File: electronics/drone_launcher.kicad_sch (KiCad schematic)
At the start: 30 parts, among them J1 Servos F1, J10 I2C IMU, J11 I2C GPS, J12 I2C LCD, J13 BTNS F1R1, J14 BTNS F1R2, J15 BTNS F2R1, J16 BTNS F2R2, J17 BTNS F3R1, J18 BTNS F3R2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

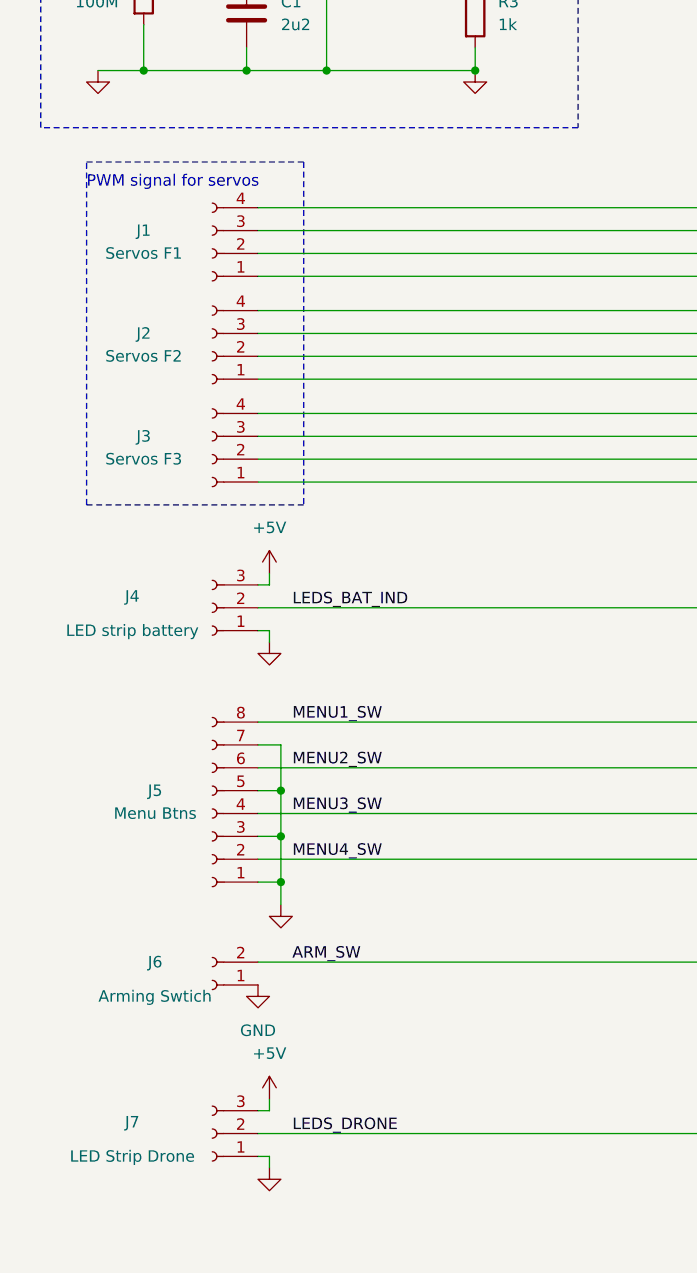
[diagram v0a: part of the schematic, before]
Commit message: added labels and initial pcb layout
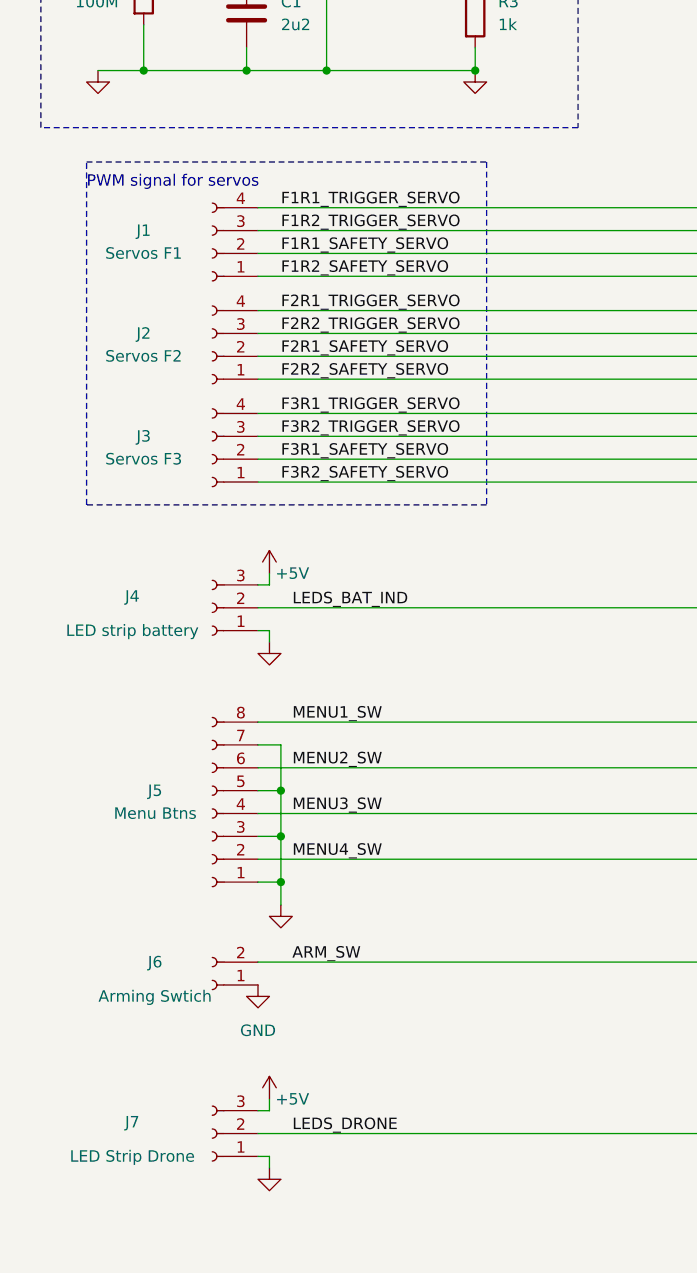
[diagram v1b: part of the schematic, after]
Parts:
- J1, J10, J11, J12, J2, J3, J8: footprint (none) -> Connector_JST:JST_XH_B4B-XH-A_1x04_P2.50mm_Vertical
- J13, J14, J15, J16, J17, J18: footprint (none) -> Connector_JST:JST_XH_B6B-XH-A_1x06_P2.50mm_Vertical
- J4, J7: footprint (none) -> Connector_JST:JST_XH_B3B-XH-A_1x03_P2.50mm_Vertical
- J5: footprint (none) -> Connector_JST:JST_XH_B8B-XH-A_1x08_P2.50mm_Vertical
- J6, J9: footprint (none) -> Connector_JST:JST_XH_B2B-XH-A_1x02_P2.50mm_Vertical
- U2: footprint (none) -> teensy:Teensy41
- U3: footprint (none) -> Adafruit_MCP23017_Breakout:Adafruit_MCP23017_Breakout
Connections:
- net F2R2_SAFETY_SERVO: now reaches J2.1 (Pin_1), U2.7 (5_IN2)
- net F2R1_SAFETY_SERVO: now reaches J2.2 (Pin_2), U2.6 (4_BCLK2)
- net F2R2_TRIGGER_SERVO: now reaches J2.3 (Pin_3), U2.5 (3_LRCLK2)
- net F2R1_TRIGGER_SERVO: now reaches J2.4 (Pin_4), U2.4 (2_OUT2)
- net F3R2_SAFETY_SERVO: now reaches J3.1 (Pin_1), U2.11 (9_OUT1C)
- net F3R1_SAFETY_SERVO: now reaches J3.2 (Pin_2), U2.10 (8_TX2_IN1)
- net F3R2_TRIGGER_SERVO: now reaches J3.3 (Pin_3), U2.9 (7_RX2_OUT1A)
- net F3R1_TRIGGER_SERVO: now reaches J3.4 (Pin_4), U2.8 (6_OUT1D)
- net F1R1_TRIGGER_SERVO: now reaches J1.4 (Pin_4), U2.36 (14_A0_TX3_SPDIF_OUT)
- net F1R2_TRIGGER_SERVO: now reaches J1.3 (Pin_3), U2.37 (15_A1_RX3_SPDIF_IN)
- net F1R1_SAFETY_SERVO: now reaches J1.2 (Pin_2), U2.44 (22_A8_CTX1)
- net F1R2_SAFETY_SERVO: now reaches J1.1 (Pin_1), U2.45 (23_A9_CRX1_MCLK1)
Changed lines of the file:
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@@
     (fill (type none))
   )
-  (rectangle (start 22.86 74.93) (end 46.99 113.03)
+  (rectangle (start 22.86 74.93) (end 67.31 113.03)
     (stroke (width 0) (type dash))
     (fill (type none))
@@
     (effects (font (size 1.27 1.27)) (justify left bottom))
   )
+  (label "F2R2_TRIGGER_SERVO" (at 44.45 93.98 0) (fields_autoplaced)
+    (effects (font (size 1.27 1.27)) (justify left bottom))
+  )
   (label "F3R1_SAFETY_SW" (at 354.33 173.99 0) (fields_autoplaced)
     (effects (font (size 1.27 1.27)) (justify left bottom))
@@
     (effects (font (size 1.27 1.27)) (justify left bottom))
   )
+  (label "F2R1_TRIGGER_SERVO" (at 44.45 91.44 0) (fields_autoplaced)
+    (effects (font (size 1.27 1.27)) (justify left bottom))
+  )
   (label "F3R2_TOP_SW" (at 354.33 189.23 0) (fields_autoplaced)
     (effects (font (size 1.27 1.27)) (justify left bottom))
@@
     (effects (font (size 1.27 1.27)) (justify left bottom))
   )
+  (label "F3R1_SAFETY_SERVO" (at 44.45 107.95 0) (fields_autoplaced)
+    (effects (font (size 1.27 1.27)) (justify left bottom))
+  )
   (label "SCL" (at 231.14 68.58 0) (fields_autoplaced)
     (effects (font (size 1.27 1.27)) (justify left bottom))
@@
     (effects (font (size 1.27 1.27)) (justify left bottom))
   )
+  (label "F3R2_SAFETY_SERVO" (at 44.45 110.49 0) (fields_autoplaced)
+    (effects (font (size 1.27 1.27)) (justify left bottom))
+  )
   (label "F2R2_SAFETY_SW" (at 257.81 229.87 0) (fields_autoplaced)
     (effects (font (size 1.27 1.27)) (justify left bottom))
@@
     (effects (font (size 1.27 1.27)) (justify left bottom))
   )
+  (label "F2R2_SAFETY_SERVO" (at 44.45 99.06 0) (fields_autoplaced)
+    (effects (font (size 1.27 1.27)) (justify left bottom))
+  )
   (label "MENU3_SW" (at 45.72 147.32 0) (fields_autoplaced)
     (effects (font (size 1.27 1.27)) (justify left bottom))
@@
   )
   (label "LEDS_BAT_IND" (at 45.72 124.46 0) (fields_autoplaced)
+    (effects (font (size 1.27 1.27)) (justify left bottom))
+  )
+  (label "F1R1_SAFETY_SERVO" (at 44.45 85.09 0) (fields_autoplaced)
     (effects (font (size 1.27 1.27)) (justify left bottom))
   )
@@
     (effects (font (size 1.27 1.27)) (justify left bottom))
   )
+  (label "F2R1_SAFETY_SERVO" (at 44.45 96.52 0) (fields_autoplaced)
+    (effects (font (size 1.27 1.27)) (justify left bottom))
+  )
+  (label "F1R1_TRIGGER_SERVO" (at 44.45 80.01 0) (fields_autoplaced)
+    (effects (font (size 1.27 1.27)) (justify left bottom))
+  )
   (label "MENU2_SW" (at 45.72 142.24 0) (fields_autoplaced)
     (effects (font (size 1.27 1.27)) (justify left bottom))
@@
   )
   (label "F1R1_TOP_SW" (at 354.33 76.2 0) (fields_autoplaced)
+    (effects (font (size 1.27 1.27)) (justify left bottom))
+  )
+  (label "F1R2_SAFETY_SERVO" (at 44.45 87.63 0) (fields_autoplaced)
     (effects (font (size 1.27 1.27)) (justify left bottom))
   )
@@
     (effects (font (size 1.27 1.27)) (justify left bottom))
   )
+  (label "F1R2_TRIGGER_SERVO" (at 44.45 82.55 0) (fields_autoplaced)
+    (effects (font (size 1.27 1.27)) (justify left bottom))
+  )
   (label "MENU4_SW" (at 45.72 152.4 0) (fields_autoplaced)
     (effects (font (size 1.27 1.27)) (justify left bottom))
@@
   )
   (label "MENU1_SW" (at 45.72 137.16 0) (fields_autoplaced)
+    (effects (font (size 1.27 1.27)) (justify left bottom))
+  )
+  (label "F3R2_TRIGGER_SERVO" (at 44.45 105.41 0) (fields_autoplaced)
+    (effects (font (size 1.27 1.27)) (justify left bottom))
+  )
+  (label "F3R1_TRIGGER_SERVO" (at 44.45 102.87 0) (fields_autoplaced)
     (effects (font (size 1.27 1.27)) (justify left bottom))
   )
@@
       (effects (font (size 1.27 1.27)))
     )
-    (property "Footprint" "" (at 287.02 46.99 0)
+    (property "Footprint" "Connector_JST:JST_XH_B4B-XH-A_1x04_P2.50mm_Vertical" (at 287.02 46.99 0)
       (effects (font (size 1.27 1.27)) hide)
     )
@@
       (effects (font (size 1.27 1.27)))
     )
-    (property "Footprint" "" (at 36.83 96.52 0)
+    (property "Footprint" "Connector_JST:JST_XH_B4B-XH-A_1x04_P2.50mm_Vertical" (at 36.83 96.52 0)
       (effects (font (size 1.27 1.27)) hide)
     )
@@
       (effects (font (size 1.27 1.27)))
     )
-    (property "Footprint" "" (at 36.83 107.95 0)
+    (property "Footprint" "Connector_JST:JST_XH_B4B-XH-A_1x04_P2.50mm_Vertical" (at 36.83 107.95 0)
       (effects (font (size 1.27 1.27)) hide)
     )
@@
       (effects (font (size 1.27 1.27)) (justify left))
     )
-    (property "Footprint" "" (at 378.46 173.99 0)
+    (property "Footprint" "Connector_JST:JST_XH_B6B-XH-A_1x06_P2.50mm_Vertical" (at 378.46 173.99 0)
       (effects (font (size 1.27 1.27)) hide)
     )
@@
       (effects (font (size 1.27 1.27)))
     )
-    (property "Footprint" "" (at 36.83 182.88 0)
+    (property "Footprint" "Connector_JST:JST_XH_B3B-XH-A_1x03_P2.50mm_Vertical" (at 36.83 182.88 0)
       (effects (font (size 1.27 1.27)) hide)
     )
@@
       (effects (font (size 1.27 1.27)) (justify left))
     )
-    (property "Footprint" "" (at 378.46 149.86 0)
+    (property "Footprint" "Connector_JST:JST_XH_B6B-XH-A_1x06_P2.50mm_Vertical" (at 378.46 149.86 0)
       (effects (font (size 1.27 1.27)) hide)
     )
@@
       (effects (font (size 1.27 1.27)))
     )
-    (property "Footprint" "" (at 299.72 46.99 0)
+    (property "Footprint" "Connector_JST:JST_XH_B4B-XH-A_1x04_P2.50mm_Vertical" (at 299.72 46.99 0)
       (effects (font (size 1.27 1.27)) hide)
     )
@@
       (effects (font (size 1.27 1.27)) (justify left))
     )
-    (property "Footprint" "" (at 378.46 101.6 0)
+    (property "Footprint" "Connector_JST:JST_XH_B6B-XH-A_1x06_P2.50mm_Vertical" (at 378.46 101.6 0)
       (effects (font (size 1.27 1.27)) hide)
     )
@@
       (effects (font (size 1.27 1.27)) (justify left))
     )
-    (property "Footprint" "" (at 378.46 81.28 0)
+    (property "Footprint" "Connector_JST:JST_XH_B6B-XH-A_1x06_P2.50mm_Vertical" (at 378.46 81.28 0)
       (effects (font (size 1.27 1.27)) hide)
     )
@@
       (effects (font (size 1.27 1.27)))
     )
-    (property "Footprint" "" (at 36.83 166.37 0)
+    (property "Footprint" "Connector_JST:JST_XH_B2B-XH-A_1x02_P2.50mm_Vertical" (at 36.83 166.37 0)
       (effects (font (size 1.27 1.27)) hide)
     )
@@
       (effects (font (size 1.27 1.27)))
     )
-    (property "Footprint" "" (at 243.84 46.99 0)
+    (property "Footprint" "Connector_JST:JST_XH_B4B-XH-A_1x04_P2.50mm_Vertical" (at 243.84 46.99 0)
       (effects (font (size 1.27 1.27)) hide)
     )
@@
       (effects (font (size 1.27 1.27)) (justify right))
     )
-    (property "Footprint" "" (at 256.54 46.99 0)
+    (property "Footprint" "Connector_JST:JST_XH_B2B-XH-A_1x02_P2.50mm_Vertical" (at 256.54 46.99 0)
       (effects (font (size 1.27 1.27)) hide)
     )
@@
       (effects (font (size 1.27 1.27)))
     )
-    (property "Footprint" "" (at 36.83 124.46 0)
+    (property "Footprint" "Connector_JST:JST_XH_B3B-XH-A_1x03_P2.50mm_Vertical" (at 36.83 124.46 0)
       (effects (font (size 1.27 1.27)) hide)
     )
@@
   )
   (symbol (lib_id "power:+5V") (at 43.18 179.07 0) (unit 1)
-    (in_bom yes) (on_board yes) (dnp no) (fields_autoplaced)
+    (in_bom yes) (on_board yes) (dnp no)
     (property "Reference" "#PWR06" (at 43.18 182.88 0)
       (effects (font (size 1.27 1.27)) hide)
     )
-    (property "Value" "+5V" (at 43.18 173.99 0)
+    (property "Value" "+5V" (at 45.72 179.07 0)
       (effects (font (size 1.27 1.27)))
     )
@@
       (effects (font (size 1.27 1.27)))
     )
-    (property "Footprint" "" (at 273.05 46.99 0)
+    (property "Footprint" "Connector_JST:JST_XH_B4B-XH-A_1x04_P2.50mm_Vertical" (at 273.05 46.99 0)
       (effects (font (size 1.27 1.27)) hide)
     )
@@
   )
   (symbol (lib_id "power:+5V") (at 43.18 120.65 0) (unit 1)
-    (in_bom yes) (on_board yes) (dnp no) (fields_autoplaced)
+    (in_bom yes) (on_board yes) (dnp no)
     (property "Reference" "#PWR04" (at 43.18 124.46 0)
       (effects (font (size 1.27 1.27)) hide)
     )
-    (property "Value" "+5V" (at 43.18 115.57 0)
+    (property "Value" "+5V" (at 45.72 120.65 0)
       (effects (font (size 1.27 1.27)))
     )
@@
       (effects (font (size 1.27 1.27)))
     )
-    (property "Footprint" "" (at 158.75 128.27 0)
+    (property "Footprint" "teensy:Teensy41" (at 158.75 128.27 0)
       (effects (font (size 1.27 1.27)) hide)
     )
@@
       (effects (font (size 1.27 1.27)))
     )
-    (property "Footprint" "" (at 36.83 85.09 0)
+    (property "Footprint" "Connector_JST:JST_XH_B4B-XH-A_1x04_P2.50mm_Vertical" (at 36.83 85.09 0)
       (effects (font (size 1.27 1.27)) hide)
     )
@@
       (effects (font (size 1.27 1.27)) (justify left))
     )
-    (property "Footprint" "" (at 378.46 129.54 0)
+    (property "Footprint" "Connector_JST:JST_XH_B6B-XH-A_1x06_P2.50mm_Vertical" (at 378.46 129.54 0)
       (effects (font (size 1.27 1.27)) hide)
     )
@@
       (effects (font (size 1.27 1.27)))
     )
-    (property "Footprint" "" (at 36.83 147.32 0)
+    (property "Footprint" "Connector_JST:JST_XH_B8B-XH-A_1x08_P2.50mm_Vertical" (at 40.64 157.48 0)
       (effects (font (size 1.27 1.27)) hide)
     )
@@
       (effects (font (size 1.27 1.27)) (justify left))
     )
-    (property "Footprint" "" (at 378.46 194.31 0)
+    (property "Footprint" "Connector_JST:JST_XH_B6B-XH-A_1x06_P2.50mm_Vertical" (at 378.46 194.31 0)
       (effects (font (size 1.27 1.27)) hide)
     )
@@
       (effects (font (size 1.27 1.27)))
     )
-    (property "Footprint" "" (at 279.4 203.2 0)
-      (effects (font (size 1.27 1.27)) hide)
-    )
+    (property "Footprint" "Adafruit_MCP23017_Breakout:Adafruit_MCP23017_Breakout" (at 279.4 203.2 0)
+      (effects (font (size 1.27 1.27)) hide)
+    )

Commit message: improved routing and new footprints
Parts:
- removed 111, 112, 12: ~, drone_launcher:MOUNTINGHOLE_3.0_PLATED_VIAS, symbol drone_launcher-eagle-import:MOUNTINGHOLE
- added J19: GPS, Connector_JST:JST_XH_B6B-XH-A_1x06_P2.50mm_Vertical, symbol Connector:Conn_01x06_Socket
- added J20: XT60-M, AMASS_XT60-M, symbol XT60-M:XT60-M
- added MH2, MH3, MH4: ~, MountingHole:MountingHole_3.2mm_M3, symbol drone_launcher-eagle-import:MOUNTINGHOLE
- C1: footprint (none) -> Capacitor_SMD:C_1206_3216Metric
- D1: footprint (none) -> LED_SMD:LED_1206_3216Metric
- J11: value I2C GPS -> I2C LCD
- J12: value I2C LCD -> I2C Extra
- MH1: renamed from 11; footprint drone_launcher:MOUNTINGHOLE_3.0_PLATED_VIAS -> MountingHole:MountingHole_3.2mm_M3
- R1, R2, R3: footprint (none) -> Resistor_SMD:R_1206_3216Metric
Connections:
- net +24V: now also J20.P (POS)
- net +5V: now also J10.1 (Pin_1), J11.1 (Pin_1), J12.1 (Pin_1), U3.1 (Vin), J19.1 (Pin_1); no longer J10.4 (Pin_4), J11.4 (Pin_4), J12.4 (Pin_4), U3.0 (Vin)
- net BAT_MEAS: now also U2.45 (23_A9_CRX1_MCLK1); no longer U2.16 (24_A10_TX6_SCL2)
- net F1R1_BOTM_SW: now also U3.21 (B5); no longer U3.19 (B7)
- net F1R1_SAFETY_SERVO: now also U2.6 (4_BCLK2); no longer U2.44 (22_A8_CTX1)
- net F1R1_SAFETY_SW: now also U3.20 (B6); no longer U2.26 (34_RX8)
- net F1R1_TOP_SW: now also U3.19 (B7); no longer U2.27 (35_TX8)
- net F1R1_TRIGGER_SERVO: now also U2.4 (2_OUT2); no longer U2.36 (14_A0_TX3_SPDIF_OUT)
- net F1R2_BOTM_SW: now also U3.24 (B2); no longer U3.22 (B4)
- net F1R2_SAFETY_SERVO: now also U2.7 (5_IN2); no longer U2.45 (23_A9_CRX1_MCLK1)
- net F1R2_SAFETY_SW: now also U3.23 (B3); no longer U3.21 (B5)
- net F1R2_TOP_SW: now also U3.22 (B4); no longer U3.20 (B6)
- net F1R2_TRIGGER_SERVO: now also U2.5 (3_LRCLK2); no longer U2.37 (15_A1_RX3_SPDIF_IN)
- net F2R1_BOTM_SW: now also U3.13 (A7); no longer U3.25 (B1)
- net F2R1_SAFETY_SERVO: now also U2.10 (8_TX2_IN1); no longer U2.6 (4_BCLK2)
- net F2R1_SAFETY_SW: now also U3.26 (B0); no longer U3.24 (B2)
- net F2R1_TRIGGER_SERVO: now also U2.8 (6_OUT1D); no longer U2.4 (2_OUT2)
- net F2R2_BOTM_SW: now also U3.10 (A4); no longer U3.12 (A6)
- net F2R2_SAFETY_SERVO: now also U2.11 (9_OUT1C); no longer U2.7 (5_IN2)
- net F2R2_SAFETY_SW: now also U3.11 (A5); no longer U3.13 (A7)
- net F2R2_TOP_SW: now also U3.12 (A6); no longer U3.26 (B0)
- net F2R2_TRIGGER_SERVO: now also U2.9 (7_RX2_OUT1A); no longer U2.5 (3_LRCLK2)
- net F2_R1_TOP_SW: now also U3.25 (B1); no longer U3.23 (B3)
- net F3R1_BOTM_SW: now also U3.7 (A1); no longer U3.9 (A3)
- net F3R1_SAFETY_SERVO: now also U2.14 (12_MISO_MQSL); no longer U2.10 (8_TX2_IN1)
- net F3R1_SAFETY_SW: now also U3.8 (A2); no longer U3.10 (A4)
- net F3R1_TOP_SW: now also U3.9 (A3); no longer U3.11 (A5)
- net F3R1_TRIGGER_SERVO: now also U2.12 (10_CS_MQSR); no longer U2.8 (6_OUT1D)
- net F3R2_BOTM_SW: now also U2.26 (34_RX8); no longer U3.6 (A0)
- net F3R2_SAFETY_SERVO: now also U2.16 (24_A10_TX6_SCL2); no longer U2.11 (9_OUT1C)
- net F3R2_SAFETY_SW: now also U2.27 (35_TX8); no longer U3.7 (A1)
- net F3R2_TOP_SW: now also U3.6 (A0); no longer U3.8 (A2)
- net F3R2_TRIGGER_SERVO: now also U2.13 (11_MOSI_CTX1); no longer U2.9 (7_RX2_OUT1A)
- net GND: now also J10.4 (Pin_4), J11.4 (Pin_4), J12.4 (Pin_4), U2.34 (GND), U3.2 (GND), J19.6 (Pin_6), J20.N (NEG); no longer J10.3 (Pin_3), J11.3 (Pin_3), J12.3 (Pin_3), U3.1 (GND)
- net SCL: now also J10.3 (Pin_3), J11.3 (Pin_3), J12.3 (Pin_3), J19.3 (Pin_3); no longer J10.2 (Pin_2), J11.2 (Pin_2), J12.2 (Pin_2)
- net SDA: now also J10.2 (Pin_2), J11.2 (Pin_2), J12.2 (Pin_2), J19.2 (Pin_2); no longer J10.1 (Pin_1), J11.1 (Pin_1), J12.1 (Pin_1)
- net GPS_RX: now reaches U2.38 (16_A2_RX4_SCL1)
- net GPS_RX: now also J19.4 (Pin_4)
- net GPS_TX: now reaches U2.39 (17_A3_TX4_SDA1)
- net GPS_TX: now also J19.5 (Pin_5)
- no-connect marks 21 -> 36
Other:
- note added: "I2C, SPI and serial connectors"
- note added: "Led strip for drone status"
- note removed: "I2C and SPI connectors"
- moved on the sheet: C1, D1, J10, J11, J12, J4, J5, J6, J7, J8, J9, R1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

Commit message: version 1.0 pcb
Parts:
- removed J12: I2C Extra, Connector_JST:JST_XH_B4B-XH-A_1x04_P2.50mm_Vertical, symbol Connector:Conn_01x04_Socket
- added D4: RED, LED_SMD:LED_1206_3216Metric, symbol Device:LED
- added D5: GREEN, LED_SMD:LED_1206_3216Metric, symbol Device:LED
- added R6, R7: 1k, Resistor_SMD:R_1206_3216Metric, symbol Device:R
- C1: value 2u2 -> 220n
- J20: value XT60-M -> PWR IN
- R1: value 800M -> 820K
- R2: value 100M -> 120K
- U2: symbol Teensy:Teensy4.1 -> Teensy:Teensy4.1_custom
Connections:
- net F2R1_BOTM_SW: now also U3.6 (A0); no longer U3.13 (A7)
- net F2R2_BOTM_SW: now also U3.9 (A3); no longer U3.10 (A4)
- net F2R2_SAFETY_SW: now also U3.8 (A2); no longer U3.11 (A5)
- net F2R2_TOP_SW: now also U3.7 (A1); no longer U3.12 (A6)
- net F3R1_BOTM_SW: now also U3.12 (A6); no longer U3.7 (A1)
- net F3R1_SAFETY_SW: now also U3.11 (A5); no longer U3.8 (A2)
- net F3R1_TOP_SW: now also U3.10 (A4); no longer U3.9 (A3)
- net F3R2_TOP_SW: now also U3.13 (A7); no longer U3.6 (A0)
- net GND: now also R6.2, R7.2
- net GPS_RX: now also J19.2 (Pin_2), U2.43 (21_A7_RX5_BCLK1); no longer J19.4 (Pin_4), U2.38 (16_A2_RX4_SCL1)
- net GPS_TX: now also J19.3 (Pin_3), U2.42 (20_A6_TX5_LRCLK1); no longer J19.5 (Pin_5), U2.39 (17_A3_TX4_SDA1)
- net SCL: now also J19.5 (Pin_5); no longer J19.3 (Pin_3)
- net SDA: now also J19.4 (Pin_4); no longer J19.2 (Pin_2)
- net LED_ALIVE: now reaches U2.28 (36_CS)
- net LED_ALIVE: now also D5.2 (A)
- net LED_DBG: now reaches U2.29 (37_CS)
- net LED_DBG: now also D4.2 (A)
- net RST_MCP: now reaches U2.36 (14_A0_TX3_SPDIF_OUT)
- net RST_MCP: now also U3.5 (RST)
- new net: D4.1 (K), R6.1
- new net: D5.1 (K), R7.1
- no-connect marks 36 -> 16
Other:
- note added: "Debug Leds"
- moved on the sheet: J19, J7
